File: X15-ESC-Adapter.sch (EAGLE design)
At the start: 10 parts, among them J1 IPBT-103-H1-T-S, J2 IPBT-103-H1-T-S, J3 IPBT-103-H1-T-S, J4 IPBT-103-H1-T-S

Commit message: Adjusted thermals
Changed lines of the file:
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@@
 <part name="J1" library="X15-ESC-Adapter" deviceset="IPBT-103-H1-T-S" device="" package3d_urn="urn:adsk.eagle:package:37886187/2"/>
 <part name="LUMENIER_ESC" library="X15-ESC-Adapter" deviceset="LUMENIER" device="" package3d_urn="urn:adsk.eagle:package:37886188/1"/>
+<part name="BACKPLANE_CONNECTIONS" library="X15-ESC-Adapter" deviceset="IPS1-112-01-L-D" device="" package3d_urn="urn:adsk.eagle:package:38090775/2"/>
 <part name="SUPPLY1" library="supply2" library_urn="urn:adsk.eagle:library:372" deviceset="GND" device=""/>
 <part name="H1" library="X15-ESC-Adapter" deviceset="6-32-HOLE" device="" package3d_urn="urn:adsk.eagle:package:37886189/1"/>
@@
 <part name="H3" library="X15-ESC-Adapter" deviceset="6-32-HOLE" device="" package3d_urn="urn:adsk.eagle:package:37886189/1"/>
 <part name="H4" library="X15-ESC-Adapter" deviceset="6-32-HOLE" device="" package3d_urn="urn:adsk.eagle:package:37886189/1"/>
-<part name="BACKPLANE_CONNECTIONS" library="X15-ESC-Adapter" deviceset="IPS1-112-01-L-D" device="" package3d_urn="urn:adsk.eagle:package:38090775/2"/>
 </parts>
 <sheets>
@@
 <attribute name="NAME" x="152.4" y="111.76" size="1.778" layer="95"/>
 </instance>
+<instance part="BACKPLANE_CONNECTIONS" gate="G$1" x="218.44" y="132.08" smashed="yes">
+<attribute name="NAME" x="215.9" y="129.54" size="1.27" layer="95" rot="R90"/>
+</instance>
 <instance part="SUPPLY1" gate="GND" x="218.44" y="104.14" smashed="yes">
 <attribute name="VALUE" x="216.535" y="100.965" size="1.778" layer="96"/>
@@
 <attribute name="NAME" x="91.44" y="132.08" size="1.016" layer="95" align="bottom-center"/>
 <attribute name="VALUE" x="91.44" y="127" size="1.016" layer="95" align="top-center"/>
-</instance>
-<instance part="BACKPLANE_CONNECTIONS" gate="G$1" x="218.44" y="132.08" smashed="yes">
-<attribute name="NAME" x="215.9" y="129.54" size="1.27" layer="95" rot="R90"/>
 </instance>
 </instances>
@@
 <net name="12V" class="0">
 <segment>
+<pinref part="BACKPLANE_CONNECTIONS" gate="G$1" pin="12V"/>
 <wire x1="218.44" y1="144.78" x2="218.44" y2="154.94" width="0.1524" layer="91"/>
 <label x="218.44" y="154.94" size="1.778" layer="95" xref="yes"/>
-<pinref part="BACKPLANE_CONNECTIONS" gate="G$1" pin="12V"/>
 </segment>
 <segment>
@@
 </segment>
 <segment>
+<pinref part="BACKPLANE_CONNECTIONS" gate="G$1" pin="GND"/>
 <wire x1="218.44" y1="119.38" x2="218.44" y2="106.68" width="0.1524" layer="91"/>
 <pinref part="SUPPLY1" gate="GND" pin="GND"/>
-<label x="218.44" y="111.76" size="1.778" layer="95" rot="R270"/>
-<pinref part="BACKPLANE_CONNECTIONS" gate="G$1" pin="GND"/>
-</segment>
-</net>
+<label x="218.44" y="106.68" size="1.778" layer="95" rot="R270"/>
+</segment>
+</net>

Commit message: Adjusted the IPBT Footprint
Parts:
- J1, J2, J3, J4: value IPBT-103-H1-T-S -> IBPT-103-H1-T-S-RA; device X15-ESC-Adapter:IPBT-103-H1-T-S -> X15-ESC-Adapter:IBPT-103-H1-T-S-RA
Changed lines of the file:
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@@
 <parts>
 <part name="FRAME1" library="SparkFun-Aesthetics" library_urn="urn:adsk.eagle:library:507" deviceset="FRAME-A4L" device=""/>
-<part name="J4" library="X15-ESC-Adapter" deviceset="IPBT-103-H1-T-S" device="" package3d_urn="urn:adsk.eagle:package:37886187/2"/>
-<part name="J3" library="X15-ESC-Adapter" deviceset="IPBT-103-H1-T-S" device="" package3d_urn="urn:adsk.eagle:package:37886187/2"/>
-<part name="J2" library="X15-ESC-Adapter" deviceset="IPBT-103-H1-T-S" device="" package3d_urn="urn:adsk.eagle:package:37886187/2"/>
-<part name="J1" library="X15-ESC-Adapter" deviceset="IPBT-103-H1-T-S" device="" package3d_urn="urn:adsk.eagle:package:37886187/2"/>
+<part name="J4" library="X15-ESC-Adapter" deviceset="IBPT-103-H1-T-S-RA" device="" package3d_urn="urn:adsk.eagle:package:38819791/3"/>
+<part name="J3" library="X15-ESC-Adapter" deviceset="IBPT-103-H1-T-S-RA" device="" package3d_urn="urn:adsk.eagle:package:38819791/3"/>
+<part name="J2" library="X15-ESC-Adapter" deviceset="IBPT-103-H1-T-S-RA" device="" package3d_urn="urn:adsk.eagle:package:38819791/3"/>
+<part name="J1" library="X15-ESC-Adapter" deviceset="IBPT-103-H1-T-S-RA" device="" package3d_urn="urn:adsk.eagle:package:38819791/3"/>
 <part name="LUMENIER_ESC" library="X15-ESC-Adapter" deviceset="LUMENIER" device="" package3d_urn="urn:adsk.eagle:package:37886188/1"/>
 <part name="BACKPLANE_CONNECTIONS" library="X15-ESC-Adapter" deviceset="IPS1-112-01-L-D" device="" package3d_urn="urn:adsk.eagle:package:38090775/2"/>
@@
 <attribute name="SHEET" x="198.12" y="3.81" size="2.54" layer="94" font="vector"/>
 </instance>
-<instance part="J4" gate="G$1" x="83.82" y="81.28" smashed="yes">
-<attribute name="NAME" x="83.82" y="91.44" size="1.778" layer="95"/>
+<instance part="J4" gate="G$1" x="88.9" y="83.82" smashed="yes">
+<attribute name="NAME" x="88.9" y="93.98" size="1.778" layer="95"/>
 </instance>
-<instance part="J3" gate="G$1" x="83.82" y="96.52" smashed="yes">
-<attribute name="NAME" x="83.82" y="106.68" size="1.778" layer="95"/>
+<instance part="J3" gate="G$1" x="88.9" y="99.06" smashed="yes">
+<attribute name="NAME" x="88.9" y="109.22" size="1.778" layer="95"/>
 </instance>
-<instance part="J2" gate="G$1" x="106.68" y="81.28" smashed="yes" rot="MR0">
-<attribute name="NAME" x="106.68" y="91.44" size="1.778" layer="95" rot="MR0"/>
+<instance part="J2" gate="G$1" x="101.6" y="83.82" smashed="yes" rot="MR0">
+<attribute name="NAME" x="101.6" y="93.98" size="1.778" layer="95" rot="MR0"/>
 </instance>
-<instance part="J1" gate="G$1" x="106.68" y="96.52" smashed="yes" rot="MR0">
-<attribute name="NAME" x="106.68" y="106.68" size="1.778" layer="95" rot="MR0"/>
+<instance part="J1" gate="G$1" x="101.6" y="99.06" smashed="yes" rot="MR0">
+<attribute name="NAME" x="101.6" y="109.22" size="1.778" layer="95" rot="MR0"/>
 </instance>
 <instance part="LUMENIER_ESC" gate="G$1" x="152.4" y="91.44" smashed="yes">

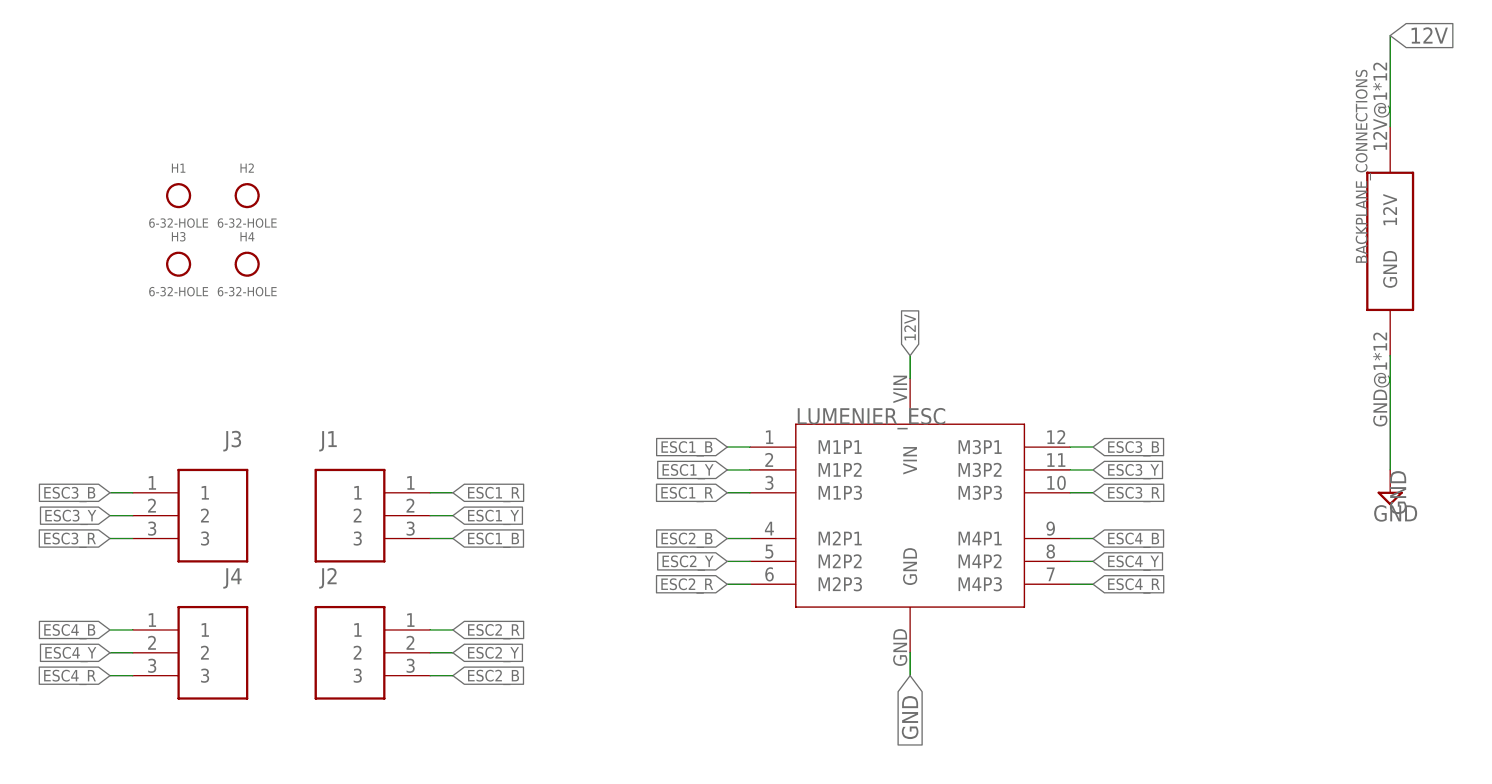
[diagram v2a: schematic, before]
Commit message: Complete ESC Adapter Design
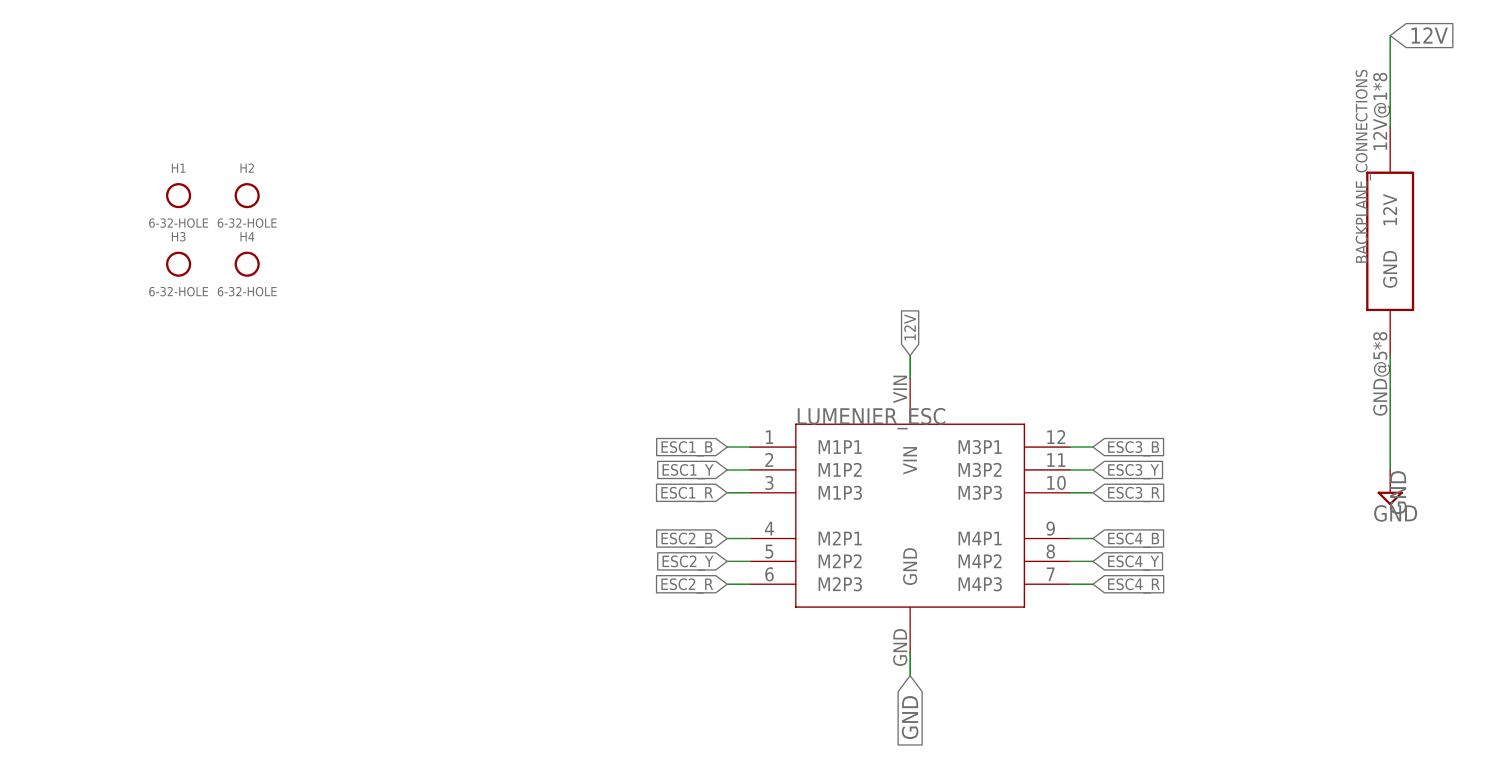
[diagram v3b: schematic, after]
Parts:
- removed J1, J2, J3, J4: IBPT-103-H1-T-S-RA, X15-ESC-Adapter:IBPT-103-H1-T-S-RA
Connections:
- net ESC1_B: no longer J1.3
- net ESC1_R: no longer J1.1
- net ESC1_Y: no longer J1.2
- net ESC2_B: no longer J2.3
- net ESC2_R: no longer J2.1
- net ESC2_Y: no longer J2.2
- net ESC3_B: no longer J3.1
- net ESC3_R: no longer J3.3
- net ESC3_Y: no longer J3.2
- net ESC4_B: no longer J4.1
- net ESC4_R: no longer J4.3
- net ESC4_Y: no longer J4.2
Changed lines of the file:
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@@
 <parts>
 <part name="FRAME1" library="SparkFun-Aesthetics" library_urn="urn:adsk.eagle:library:507" deviceset="FRAME-A4L" device=""/>
-<part name="J4" library="X15-ESC-Adapter" deviceset="IBPT-103-H1-T-S-RA" device="" package3d_urn="urn:adsk.eagle:package:38819791/3"/>
-<part name="J3" library="X15-ESC-Adapter" deviceset="IBPT-103-H1-T-S-RA" device="" package3d_urn="urn:adsk.eagle:package:38819791/3"/>
-<part name="J2" library="X15-ESC-Adapter" deviceset="IBPT-103-H1-T-S-RA" device="" package3d_urn="urn:adsk.eagle:package:38819791/3"/>
-<part name="J1" library="X15-ESC-Adapter" deviceset="IBPT-103-H1-T-S-RA" device="" package3d_urn="urn:adsk.eagle:package:38819791/3"/>
 <part name="LUMENIER_ESC" library="X15-ESC-Adapter" deviceset="LUMENIER" device="" package3d_urn="urn:adsk.eagle:package:37886188/1"/>
 <part name="BACKPLANE_CONNECTIONS" library="X15-ESC-Adapter" deviceset="IPS1-112-01-L-D" device="" package3d_urn="urn:adsk.eagle:package:38090775/2"/>
@@
 <attribute name="LAST_DATE_TIME" x="184.15" y="8.89" size="2.286" layer="94" font="vector"/>
 <attribute name="SHEET" x="198.12" y="3.81" size="2.54" layer="94" font="vector"/>
-</instance>
-<instance part="J4" gate="G$1" x="88.9" y="83.82" smashed="yes">
-<attribute name="NAME" x="88.9" y="93.98" size="1.778" layer="95"/>
-</instance>
-<instance part="J3" gate="G$1" x="88.9" y="99.06" smashed="yes">
-<attribute name="NAME" x="88.9" y="109.22" size="1.778" layer="95"/>
-</instance>
-<instance part="J2" gate="G$1" x="101.6" y="83.82" smashed="yes" rot="MR0">
-<attribute name="NAME" x="101.6" y="93.98" size="1.778" layer="95" rot="MR0"/>
-</instance>
-<instance part="J1" gate="G$1" x="101.6" y="99.06" smashed="yes" rot="MR0">
-<attribute name="NAME" x="101.6" y="109.22" size="1.778" layer="95" rot="MR0"/>
 </instance>
 <instance part="LUMENIER_ESC" gate="G$1" x="152.4" y="91.44" smashed="yes">
@@
 <label x="185.42" y="104.14" size="1.27" layer="95" xref="yes"/>
 </segment>
-<segment>
-<pinref part="J3" gate="G$1" pin="3"/>
-<wire x1="78.74" y1="99.06" x2="76.2" y2="99.06" width="0.1524" layer="91"/>
-<label x="76.2" y="99.06" size="1.27" layer="95" rot="R180" xref="yes"/>
-</segment>
 </net>
 <net name="ESC3_Y" class="0">
-<segment>
-<pinref part="J3" gate="G$1" pin="2"/>
-<wire x1="78.74" y1="101.6" x2="76.2" y2="101.6" width="0.1524" layer="91"/>
-<label x="76.2" y="101.6" size="1.27" layer="95" rot="R180" xref="yes"/>
-</segment>
 <segment>
 <pinref part="LUMENIER_ESC" gate="G$1" pin="M3P2"/>
@@
 <label x="185.42" y="109.22" size="1.27" layer="95" xref="yes"/>
 </segment>
-<segment>
-<pinref part="J3" gate="G$1" pin="1"/>
-<wire x1="78.74" y1="104.14" x2="76.2" y2="104.14" width="0.1524" layer="91"/>
-<label x="76.2" y="104.14" size="1.27" layer="95" rot="R180" xref="yes"/>
-</segment>
 </net>
 <net name="ESC4_R" class="0">
@@
 <label x="185.42" y="93.98" size="1.27" layer="95" xref="yes"/>
 </segment>
-<segment>
-<pinref part="J4" gate="G$1" pin="3"/>
-<wire x1="78.74" y1="83.82" x2="76.2" y2="83.82" width="0.1524" layer="91"/>
-<label x="76.2" y="83.82" size="1.27" layer="95" rot="R180" xref="yes"/>
-</segment>
 </net>
 <net name="ESC4_Y" class="0">
-<segment>
-<pinref part="J4" gate="G$1" pin="2"/>
-<wire x1="78.74" y1="86.36" x2="76.2" y2="86.36" width="0.1524" layer="91"/>
-<label x="76.2" y="86.36" size="1.27" layer="95" rot="R180" xref="yes"/>
-</segment>
 <segment>
 <pinref part="LUMENIER_ESC" gate="G$1" pin="M4P2"/>
@@
 <label x="185.42" y="99.06" size="1.27" layer="95" xref="yes"/>
 </segment>
-<segment>
-<pinref part="J4" gate="G$1" pin="1"/>
-<wire x1="78.74" y1="88.9" x2="76.2" y2="88.9" width="0.1524" layer="91"/>
-<label x="76.2" y="88.9" size="1.27" layer="95" rot="R180" xref="yes"/>
-</segment>
 </net>
 <net name="ESC1_B" class="0">
-<segment>
-<pinref part="J1" gate="G$1" pin="3"/>
-<wire x1="111.76" y1="99.06" x2="114.3" y2="99.06" width="0.1524" layer="91"/>
-<label x="114.3" y="99.06" size="1.27" layer="95" xref="yes"/>
-</segment>
 <segment>
 <pinref part="LUMENIER_ESC" gate="G$1" pin="M1P1"/>
@@
 <net name="ESC2_R" class="0">
 <segment>
-<pinref part="J2" gate="G$1" pin="1"/>
-<wire x1="111.76" y1="88.9" x2="114.3" y2="88.9" width="0.1524" layer="91"/>
-<label x="114.3" y="88.9" size="1.27" layer="95" xref="yes"/>
-</segment>
-<segment>
 <pinref part="LUMENIER_ESC" gate="G$1" pin="M2P3"/>
 <wire x1="147.32" y1="93.98" x2="144.78" y2="93.98" width="0.1524" layer="91"/>
@@
 </net>
 <net name="ESC2_Y" class="0">
-<segment>
-<pinref part="J2" gate="G$1" pin="2"/>
-<wire x1="111.76" y1="86.36" x2="114.3" y2="86.36" width="0.1524" layer="91"/>
-<label x="114.3" y="86.36" size="1.27" layer="95" xref="yes"/>
-</segment>
 <segment>
 <pinref part="LUMENIER_ESC" gate="G$1" pin="M2P2"/>
@@
 <net name="ESC2_B" class="0">
 <segment>
-<pinref part="J2" gate="G$1" pin="3"/>
-<wire x1="111.76" y1="83.82" x2="114.3" y2="83.82" width="0.1524" layer="91"/>
-<label x="114.3" y="83.82" size="1.27" layer="95" xref="yes"/>
-</segment>
-<segment>
 <pinref part="LUMENIER_ESC" gate="G$1" pin="M2P1"/>
 <wire x1="147.32" y1="99.06" x2="144.78" y2="99.06" width="0.1524" layer="91"/>
@@
 </net>
 <net name="ESC1_R" class="0">
-<segment>
-<pinref part="J1" gate="G$1" pin="1"/>
-<wire x1="111.76" y1="104.14" x2="114.3" y2="104.14" width="0.1524" layer="91"/>
-<label x="114.3" y="104.14" size="1.27" layer="95" xref="yes"/>
-</segment>
 <segment>
 <pinref part="LUMENIER_ESC" gate="G$1" pin="M1P3"/>
@@
 <net name="ESC1_Y" class="0">
 <segment>
-<pinref part="J1" gate="G$1" pin="2"/>
-<wire x1="111.76" y1="101.6" x2="114.3" y2="101.6" width="0.1524" layer="91"/>
-<label x="114.3" y="101.6" size="1.27" layer="95" xref="yes"/>
-</segment>
-<segment>
 <pinref part="LUMENIER_ESC" gate="G$1" pin="M1P2"/>

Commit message: Update to v2
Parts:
- removed H3, H4: 6-32-HOLE, X15-ESC-Adapter:6-32-HOLE
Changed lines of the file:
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@@
 <layers>
 <layer number="1" name="Top" color="4" fill="1" visible="no" active="no"/>
+<layer number="2" name="Route2" color="1" fill="3" visible="no" active="no"/>
+<layer number="3" name="Route3" color="4" fill="3" visible="no" active="no"/>
+<layer number="4" name="Route4" color="1" fill="4" visible="no" active="no"/>
+<layer number="5" name="Route5" color="4" fill="4" visible="no" active="no"/>
+<layer number="6" name="Route6" color="1" fill="8" visible="no" active="no"/>
+<layer number="7" name="Route7" color="4" fill="8" visible="no" active="no"/>
+<layer number="8" name="Route8" color="1" fill="2" visible="no" active="no"/>
+<layer number="9" name="Route9" color="4" fill="2" visible="no" active="no"/>
+<layer number="10" name="Route10" color="1" fill="7" visible="no" active="no"/>
+<layer number="11" name="Route11" color="4" fill="7" visible="no" active="no"/>
+<layer number="12" name="Route12" color="1" fill="5" visible="no" active="no"/>
+<layer number="13" name="Route13" color="4" fill="5" visible="no" active="no"/>
+<layer number="14" name="Route14" color="1" fill="6" visible="no" active="no"/>
+<layer number="15" name="Route15" color="4" fill="6" visible="no" active="no"/>
 <layer number="16" name="Bottom" color="1" fill="1" visible="no" active="no"/>
 <layer number="17" name="Pads" color="2" fill="1" visible="no" active="no"/>
@@
 <part name="H1" library="X15-ESC-Adapter" deviceset="6-32-HOLE" device="" package3d_urn="urn:adsk.eagle:package:37886189/1"/>
 <part name="H2" library="X15-ESC-Adapter" deviceset="6-32-HOLE" device="" package3d_urn="urn:adsk.eagle:package:37886189/1"/>
-<part name="H3" library="X15-ESC-Adapter" deviceset="6-32-HOLE" device="" package3d_urn="urn:adsk.eagle:package:37886189/1"/>
-<part name="H4" library="X15-ESC-Adapter" deviceset="6-32-HOLE" device="" package3d_urn="urn:adsk.eagle:package:37886189/1"/>
 </parts>
 <sheets>
@@
 <attribute name="VALUE" x="91.44" y="134.62" size="1.016" layer="95" align="top-center"/>
 </instance>
-<instance part="H3" gate="G$1" x="83.82" y="129.54" smashed="yes">
-<attribute name="NAME" x="83.82" y="132.08" size="1.016" layer="95" align="bottom-center"/>
-<attribute name="VALUE" x="83.82" y="127" size="1.016" layer="95" align="top-center"/>
-</instance>
-<instance part="H4" gate="G$1" x="91.44" y="129.54" smashed="yes">
-<attribute name="NAME" x="91.44" y="132.08" size="1.016" layer="95" align="bottom-center"/>
-<attribute name="VALUE" x="91.44" y="127" size="1.016" layer="95" align="top-center"/>
-</instance>
 </instances>
